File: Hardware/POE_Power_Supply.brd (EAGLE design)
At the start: 27.9 x 57.1 mm, 44 parts, among them J1 MAGJACK_SYM, J2 USB_A_SMT_FEMALE_NS, U1 POE_PSU-DP990X, U4 3.3V

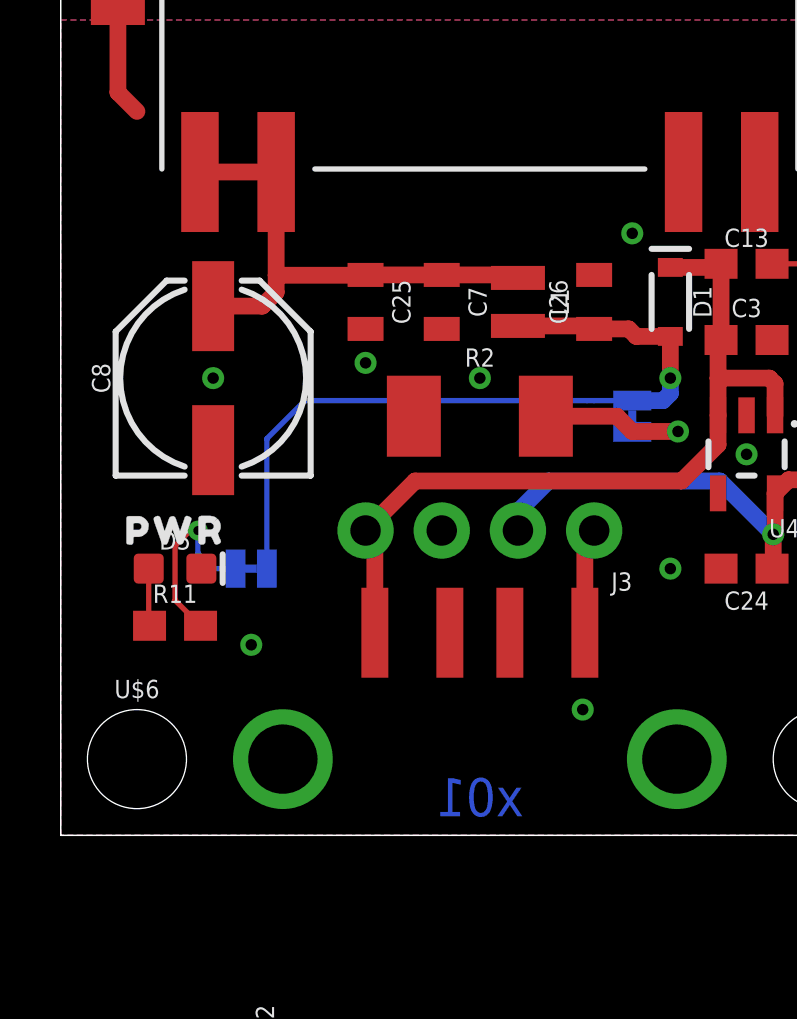
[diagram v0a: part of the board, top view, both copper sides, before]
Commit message: Add silk labels. Remove backup files. Add ignore.
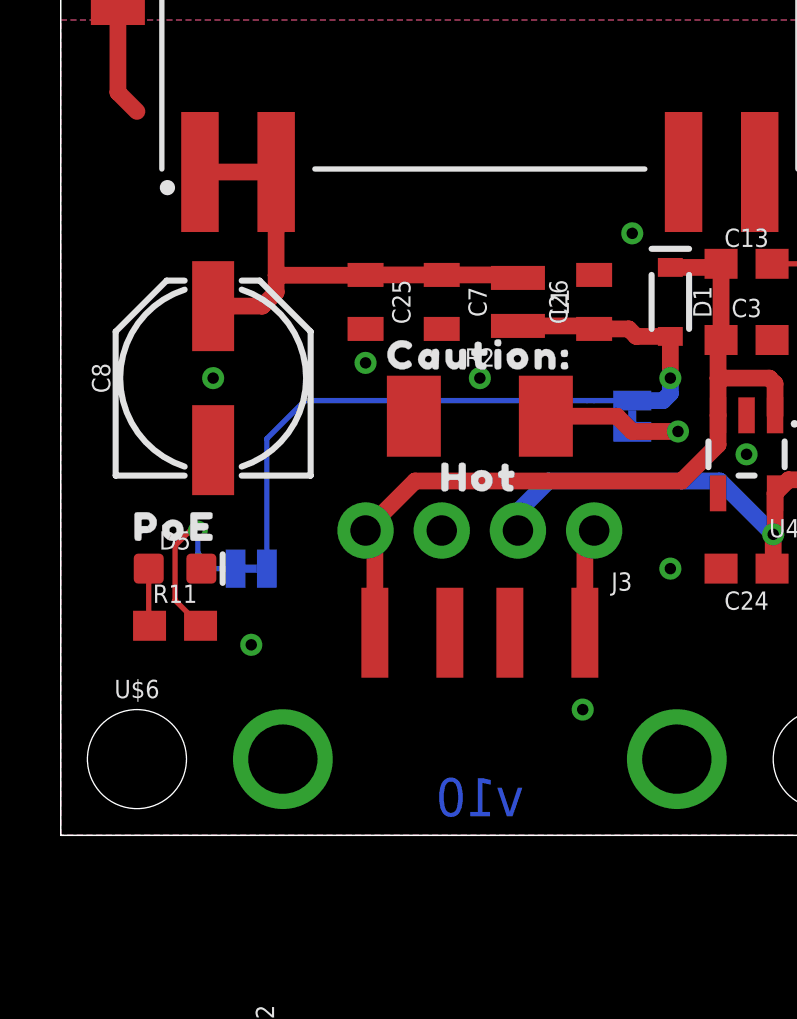
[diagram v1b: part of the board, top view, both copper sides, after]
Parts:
- removed U$7: (no value), output:PWR0
- added U$14: (no value), output:CAUTION#0
- added U$15: (no value), output:HOT1
- added U$16: (no value), output:POE0
- J1: value MAGJACK_SYM -> MAGJACK-POE; device Ethernet:MAGJACK-STR_LED -> SparkFun-Connectors:MAGJACK-SYM_LED
- LOAD, POE_LED: value (none) -> JUMPER-SMT_2_NC_TRACE_SILK
- U1: device Ethernet:DP990X -> SparkFun-IC-Power:DP990X
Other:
- board text added: "v10"
- board text removed: "x01"
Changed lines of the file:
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@@
 <layer number="37" name="tTest" color="7" fill="1" visible="no" active="yes"/>
 <layer number="38" name="bTest" color="7" fill="1" visible="no" active="yes"/>
-<layer number="39" name="tKeepout" color="4" fill="11" visible="yes" active="yes"/>
+<layer number="39" name="tKeepout" color="4" fill="11" visible="no" active="yes"/>
 <layer number="40" name="bKeepout" color="1" fill="11" visible="no" active="yes"/>
 <layer number="41" name="tRestrict" color="4" fill="10" visible="no" active="yes"/>
@@
 <layer number="44" name="Drills" color="7" fill="1" visible="no" active="yes"/>
 <layer number="45" name="Holes" color="7" fill="1" visible="yes" active="yes"/>
-<layer number="46" name="Milling" color="3" fill="1" visible="yes" active="yes"/>
+<layer number="46" name="Milling" color="3" fill="1" visible="no" active="yes"/>
 <layer number="47" name="Measures" color="7" fill="1" visible="no" active="yes"/>
 <layer number="48" name="Document" color="7" fill="1" visible="no" active="yes"/>
-<layer number="49" name="Reference" color="7" fill="1" visible="yes" active="yes"/>
+<layer number="49" name="Reference" color="7" fill="1" visible="no" active="yes"/>
 <layer number="50" name="dxf" color="7" fill="1" visible="no" active="yes"/>
 <layer number="51" name="tDocu" color="6" fill="1" visible="yes" active="yes"/>
@@
 <board>
 <plain>
-<text x="13.97" y="1.27" size="1.27" layer="16" font="vector" ratio="20" rot="SMR0" align="center">x01</text>
+<text x="13.97" y="1.27" size="1.27" layer="16" font="vector" ratio="20" rot="SMR0" align="center">v10</text>
 <text x="62.23" y="-8.89" size="1.778" layer="51" font="vector" ratio="15">N. Seidle</text>
 <wire x1="27.94" y1="0" x2="27.94" y2="57.15" width="0.05" layer="20"/>
@@
 <attribute name="VALUE" x="22.86" y="15.748" size="0.6096" layer="27" font="vector" ratio="20" align="top-center"/>
 </element>
-<element name="J1" library="Ethernet" package="MAGJACK-STR_LED" value="MAGJACK_SYM" x="13.97" y="50.8" smashed="yes" rot="R180">
+<element name="J1" library="SparkFun-Connectors" package="MAGJACK-SYM_LED" value="MAGJACK-POE" x="13.97" y="50.8" smashed="yes" rot="R180">
 <attribute name="NAME" x="13.97" y="48.66" size="0.5" layer="25" rot="R180" align="center"/>
+<attribute name="PROD_ID" value="CONN-16253" x="13.97" y="50.8" size="1.778" layer="27" rot="R180" display="off"/>
 <attribute name="VALUE" x="13.97" y="49.66" size="0.5" layer="27" rot="R180" align="center"/>
 </element>
@@
 <attribute name="NAME" x="26.162" y="12.7" size="0.6096" layer="25" font="vector" ratio="20" rot="R270" align="bottom-center"/>
 <attribute name="PROD_ID" value="RES-00818" x="25.4" y="12.7" size="1.778" layer="27" font="vector" ratio="15" rot="R270" display="off"/>
-<attribute name="VALUE" x="24.638" y="12.7" size="0.6096" layer="27" font="vector" ratio="20" rot="R270" align="top-center"/>
+<attribute name="VALUE" x="26.924" y="12.573" size="0.6096" layer="27" font="vector" ratio="20" rot="R270" align="top-center"/>
 </element>
 <element name="U4" library="SparkFun-IC-Power" package="SOT23-5" value="3.3V" x="22.86" y="12.7" smashed="yes" rot="R180">
 <attribute name="NAME" x="24.638" y="10.541" size="0.6096" layer="25" ratio="20" rot="R180"/>
 <attribute name="PROD_ID" value="VREG-12457" x="22.86" y="12.7" size="1.778" layer="27" font="vector" ratio="15" rot="R180" display="off"/>
-<attribute name="VALUE" x="24.638" y="15.494" size="0.6096" layer="27" ratio="20" rot="R180"/>
+<attribute name="VALUE" x="23.622" y="12.954" size="0.6096" layer="27" ratio="20" rot="R180"/>
 </element>
 <element name="C19" library="SparkFun-Capacitors" package="1206" value="1nF" x="1.905" y="29.21" smashed="yes" rot="R270">
@@
 <attribute name="VALUE" x="2.54" y="0.508" size="0.6096" layer="27" font="vector" ratio="20" align="top-center"/>
 </element>
-<element name="U1" library="Ethernet" package="DP990X" value="POE_PSU-DP990X" x="13.97" y="29.21" smashed="yes">
+<element name="U1" library="SparkFun-IC-Power" package="DP990X" value="POE_PSU-DP990X" x="13.97" y="29.21" smashed="yes">
 <attribute name="NAME" x="13.97" y="30.21" size="0.5" layer="25" align="center"/>
+<attribute name="PROD_ID" value="IC-16251" x="13.97" y="29.21" size="1.778" layer="27" display="off"/>
 <attribute name="VALUE" x="13.97" y="29.21" size="0.5" layer="27" align="center"/>
 </element>
@@
 <attribute name="NAME" x="16.891" y="17.78" size="0.6096" layer="25" font="vector" ratio="20" rot="R90" align="bottom-center"/>
 <attribute name="PROD_ID" value="CAP-14259" x="24.13" y="-3.81" size="1.778" layer="27" font="vector" ratio="15" rot="R90" display="off"/>
-<attribute name="VALUE" x="18.669" y="17.78" size="0.6096" layer="27" font="vector" ratio="20" rot="R90" align="top-center"/>
-</element>
-<element name="LOAD" library="SparkFun-Jumpers" package="SMT-JUMPER_2_NC_TRACE_SILK" package3d_urn="urn:adsk.eagle:package:39281/1" value="" x="19.05" y="13.97" smashed="yes" rot="MR90">
+<attribute name="VALUE" x="16.383" y="17.78" size="0.6096" layer="27" font="vector" ratio="20" rot="R90" align="top-center"/>
+</element>
+<element name="LOAD" library="SparkFun-Jumpers" package="SMT-JUMPER_2_NC_TRACE_SILK" package3d_urn="urn:adsk.eagle:package:39281/1" value="JUMPER-SMT_2_NC_TRACE_SILK" x="19.05" y="13.97" smashed="yes" rot="MR90">
 <attribute name="NAME" x="20.193" y="13.97" size="0.6096" layer="26" font="vector" ratio="20" rot="MR90" align="bottom-center"/>
 <attribute name="VALUE" x="17.907" y="13.97" size="0.6096" layer="28" font="vector" ratio="20" rot="MR90" align="top-center"/>
@@
 <attribute name="VALUE" x="13.97" y="12.319" size="0.6096" layer="27" font="vector" ratio="20" align="top-center"/>
 </element>
-<element name="POE_LED" library="SparkFun-Jumpers" package="SMT-JUMPER_2_NC_TRACE_SILK" package3d_urn="urn:adsk.eagle:package:39281/1" value="" x="6.35" y="8.89" smashed="yes" rot="MR180">
+<element name="POE_LED" library="SparkFun-Jumpers" package="SMT-JUMPER_2_NC_TRACE_SILK" package3d_urn="urn:adsk.eagle:package:39281/1" value="JUMPER-SMT_2_NC_TRACE_SILK" x="6.35" y="8.89" smashed="yes" rot="MR180">
 <attribute name="NAME" x="6.35" y="7.747" size="0.6096" layer="26" font="vector" ratio="20" rot="MR180" align="bottom-center"/>
 <attribute name="VALUE" x="6.35" y="10.033" size="0.6096" layer="28" font="vector" ratio="20" rot="MR180" align="top-center"/>
@@
 <attribute name="VALUE" x="3.81" y="8.255" size="0.6096" layer="27" font="vector" ratio="20" align="top-center"/>
 </element>
-<element name="U$7" library="output" package="PWR0" value="" x="3.81" y="10.16" smashed="yes"/>
 <element name="U$8" library="output" package="#LED#0" value="" x="6.35" y="10.795" smashed="yes" rot="MR0"/>
 <element name="U$9" library="output" package="#LOAD#0" value="" x="22.606" y="13.97" smashed="yes" rot="MR0"/>
@@
 <element name="U$12" library="output" package="#GND#1" value="" x="12.7" y="7.366" smashed="yes" rot="MR270"/>
 <element name="U$13" library="output" package="#GND#1" value="" x="17.78" y="7.366" smashed="yes" rot="MR270"/>
+<element name="U$14" library="output" package="CAUTION#0" value="" x="13.97" y="16.002" smashed="yes"/>
+<element name="U$15" library="output" package="HOT1" value="" x="13.97" y="11.938" smashed="yes"/>
+<element name="U$16" library="output" package="POE0" value="" x="3.81" y="10.287" smashed="yes"/>
 </elements>
 <signals>
@@
 <via x="20.32" y="8.89" extent="1-16" drill="0.381"/>
 <via x="17.399" y="4.191" extent="1-16" drill="0.381"/>
+<wire x1="23.71" y1="19.05" x2="25.4" y2="19.05" width="0" layer="19" extent="1-1"/>
+<wire x1="25.4" y1="16.51" x2="25.4" y2="19.05" width="0" layer="19" extent="1-1"/>
+<wire x1="23.71" y1="16.51" x2="25.4" y2="16.51" width="0" layer="19" extent="1-1"/>
+<wire x1="22.86" y1="14.0001" x2="23.71" y2="16.51" width="0" layer="19" extent="1-1"/>
+<wire x1="22.86" y1="12.7" x2="22.86" y2="14.0001" width="0" layer="19" extent="1-1"/>
+<wire x1="22.01" y1="8.89" x2="22.86" y2="12.7" width="0" layer="19" extent="1-1"/>
+<wire x1="20.32" y1="8.89" x2="22.01" y2="8.89" width="0" layer="19" extent="1-1"/>
+<wire x1="17.78" y1="10.16" x2="20.32" y2="8.89" width="0" layer="19" extent="1-1"/>
+<wire x1="17.399" y1="4.191" x2="17.47" y2="6.752" width="0" layer="19" extent="1-1"/>
+<wire x1="20.76" y1="22.11" x2="23.71" y2="19.05" width="0" layer="19" extent="1-1"/>
+<wire x1="19.05" y1="20.066" x2="20.76" y2="22.11" width="0" layer="19" extent="1-1"/>
+<wire x1="17.78" y1="18.68" x2="19.05" y2="20.066" width="0" layer="19" extent="1-1"/>
+<wire x1="12.7" y1="10.16" x2="17.78" y2="10.16" width="0" layer="19" extent="1-1"/>
+<wire x1="11.77" y1="13.97" x2="12.7" y2="10.16" width="0" layer="19" extent="1-1"/>
+<wire x1="10.16" y1="15.748" x2="11.77" y2="13.97" width="0" layer="19" extent="1-1"/>
+<wire x1="10.16" y1="16.88" x2="10.16" y2="15.748" width="0" layer="19" extent="1-1"/>
+<wire x1="12.7" y1="16.88" x2="10.16" y2="16.88" width="0" layer="19" extent="1-1"/>
+<wire x1="13.97" y1="15.24" x2="12.7" y2="16.88" width="0" layer="19" extent="1-1"/>
+<wire x1="5.08" y1="15.24" x2="10.16" y2="15.748" width="0" layer="19" extent="1-1"/>
+<wire x1="5.08" y1="12.84" x2="5.08" y2="15.24" width="0" layer="19" extent="1-1"/>
+<wire x1="4.687" y1="8.89" x2="5.08" y2="12.84" width="0" layer="19" extent="1-1"/>
+<wire x1="6.35" y1="6.35" x2="4.687" y2="8.89" width="0" layer="19" extent="1-1"/>
+<wire x1="2.54" y1="24.13" x2="5.08" y2="15.24" width="0" layer="19" extent="1-1"/>
 </signal>
 <signal name="3.3V">

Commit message: Add dims.
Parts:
- moved FRAME1 30.6 mm to (-8.89, -20.3)
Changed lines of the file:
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@@
 <layer number="47" name="Measures" color="7" fill="1" visible="no" active="yes"/>
 <layer number="48" name="Document" color="7" fill="1" visible="no" active="yes"/>
-<layer number="49" name="Reference" color="7" fill="1" visible="no" active="yes"/>
+<layer number="49" name="Reference" color="7" fill="1" visible="yes" active="yes"/>
 <layer number="50" name="dxf" color="7" fill="1" visible="no" active="yes"/>
 <layer number="51" name="tDocu" color="6" fill="1" visible="yes" active="yes"/>
@@
 <plain>
 <text x="13.97" y="1.27" size="1.27" layer="16" font="vector" ratio="20" rot="SMR0" align="center">v10</text>
-<text x="62.23" y="-8.89" size="1.778" layer="51" font="vector" ratio="15">N. Seidle</text>
+<text x="17.78" y="-20.32" size="1.778" layer="51" font="vector" ratio="15">N. Seidle</text>
 <wire x1="27.94" y1="0" x2="27.94" y2="57.15" width="0.05" layer="20"/>
 <wire x1="27.94" y1="57.15" x2="0" y2="57.15" width="0.05" layer="20"/>
@@
 <wire x1="11.935" y1="29.19" x2="1.968" y2="29.19" width="0.6" layer="46"/>
 <wire x1="25.905" y1="29.19" x2="15.938" y2="29.19" width="0.6" layer="46"/>
+<dimension x1="0" y1="0" x2="0" y2="57.15" x3="-6.35" y3="28.575" textsize="1.778" textratio="15" layer="47" unit="inch"/>
+<dimension x1="0" y1="57.15" x2="27.94" y2="57.15" x3="13.97" y3="66.04" textsize="1.778" textratio="15" layer="47" unit="inch"/>
+<dimension x1="13.97" y1="50.8" x2="0" y2="50.8" x3="6.985" y3="62.23" textsize="1.778" textratio="15" layer="47" unit="inch"/>
+<dimension x1="21.844" y1="61.468" x2="21.844" y2="57.15" x3="31.242" y3="59.309" textsize="1.778" textratio="15" layer="47" unit="inch"/>
+<dimension x1="0" y1="0" x2="13.97" y2="0" x3="6.985" y3="-11.43" textsize="1.778" textratio="15" layer="47" unit="inch"/>
+<dimension x1="20.574" y1="-7.747" x2="20.574" y2="0" x3="31.75" y3="-3.8735" textsize="1.778" textratio="15" layer="47" unit="inch"/>
+<dimension x1="2.54" y1="2.54" x2="0" y2="2.54" x3="1.27" y3="-3.81" textsize="1.778" textratio="15" layer="47" unit="inch"/>
 </plain>
 <attributes>
@@
 <element name="U$1" library="output" package="ETHERNET0" value="" x="13.97" y="19.86" smashed="yes" rot="MR0"/>
 <element name="U$2" library="output" package="#POE#0" value="" x="13.97" y="17.32" smashed="yes" rot="MR0"/>
-<element name="FRAME1" library="SparkFun-Aesthetics" package="CREATIVE_COMMONS" value="FRAME-LETTER" x="21.59" y="-17.78" smashed="yes">
-<attribute name="DESIGNER" value="" x="21.59" y="-17.78" size="1.778" layer="27" font="vector" ratio="15" display="off"/>
-<attribute name="REV" value="" x="21.59" y="-17.78" size="1.778" layer="27" font="vector" ratio="15" display="off"/>
+<element name="FRAME1" library="SparkFun-Aesthetics" package="CREATIVE_COMMONS" value="FRAME-LETTER" x="-8.89" y="-20.32" smashed="yes">
+<attribute name="DESIGNER" value="" x="-8.89" y="-20.32" size="1.778" layer="27" font="vector" ratio="15" display="off"/>
+<attribute name="REV" value="" x="-8.89" y="-20.32" size="1.778" layer="27" font="vector" ratio="15" display="off"/>
 </element>
 <element name="J2" library="SparkFun-Connectors" package="USB-A-S-NOSILK-FEMALE" value="USB_A_SMT_FEMALE_NS" x="13.97" y="0" smashed="yes" rot="R90">
